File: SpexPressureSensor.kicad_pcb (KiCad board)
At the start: 2 copper layers, 51 x 51 mm, 62 parts, among them J1 3PinJumper, J2 edgeMountSMA, P1 CONN_6, P2 NICHROME, P3 TC2030-CTX, Q1 IRLL3303PbF, Q2 MOS_N_numbered, Q3 MOS_N_numbered, Q4 MMBT4403, Q5 MOS_N_numbered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

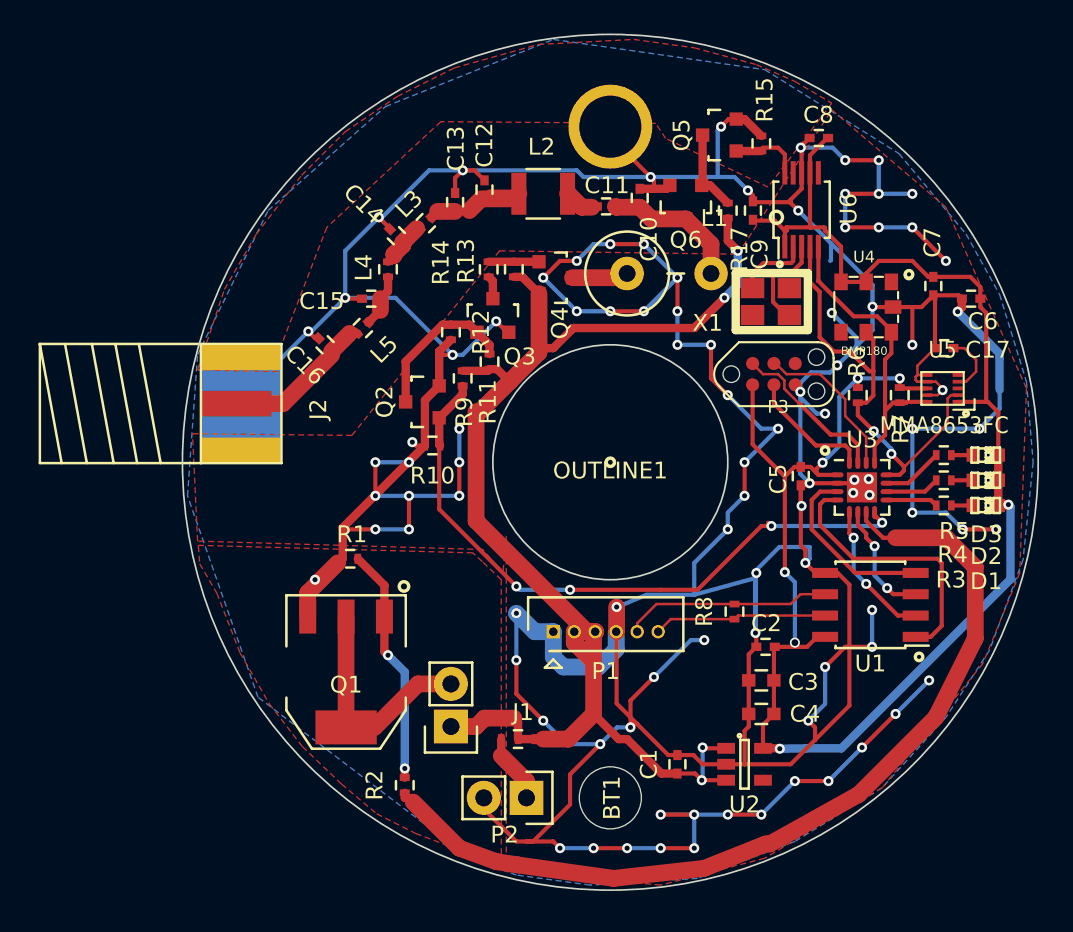
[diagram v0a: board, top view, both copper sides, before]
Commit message: Moved some traces around.
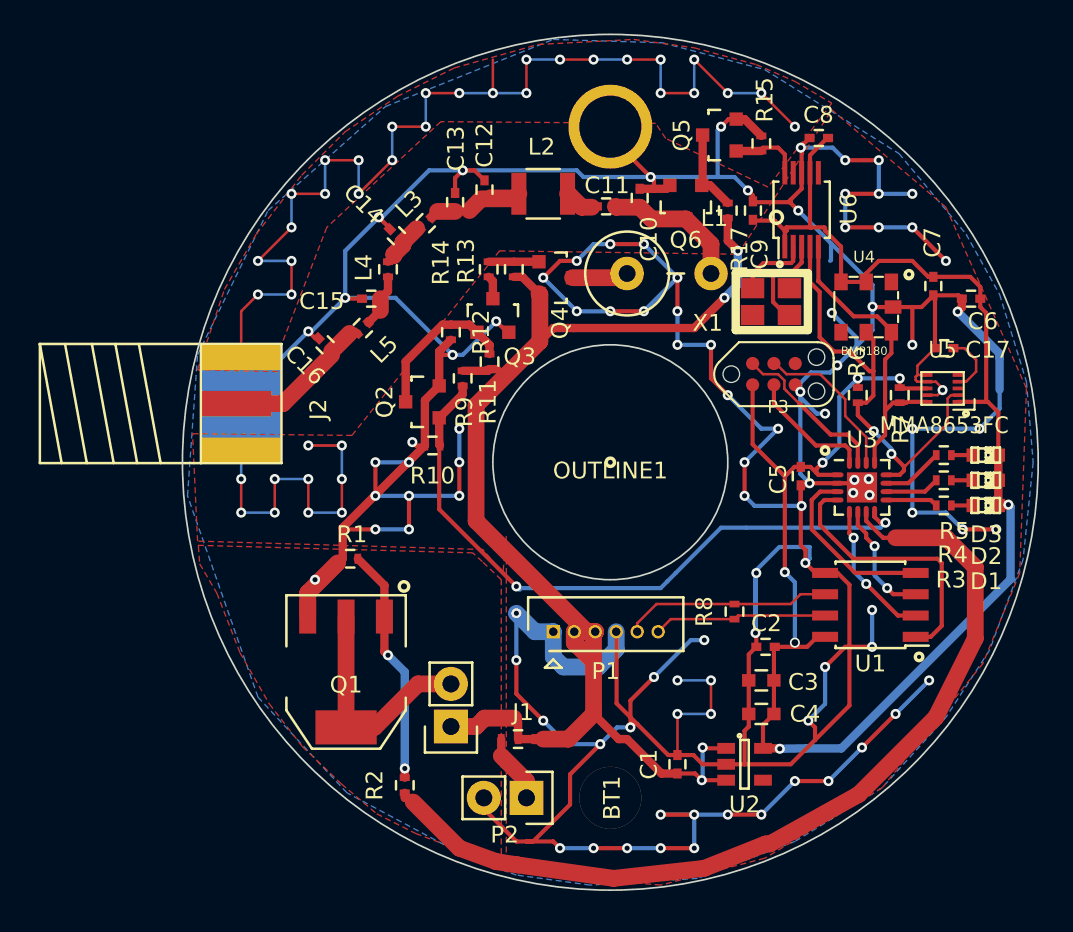
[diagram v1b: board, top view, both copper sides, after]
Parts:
- OUTLINE1: footprint PlugOutline:PLUG_OUTLINE -> PLUG_OUTLINE
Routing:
- net GND: track 414.7 -> 494.8 mm, vias 95 -> 135
- net /Beacon/12V: track 73.3 -> 71.9 mm
- net /Beacon/KEY: track 39.4 -> 40.0 mm, vias 4 -> 2

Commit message: Added a current monitor on the nichrome.
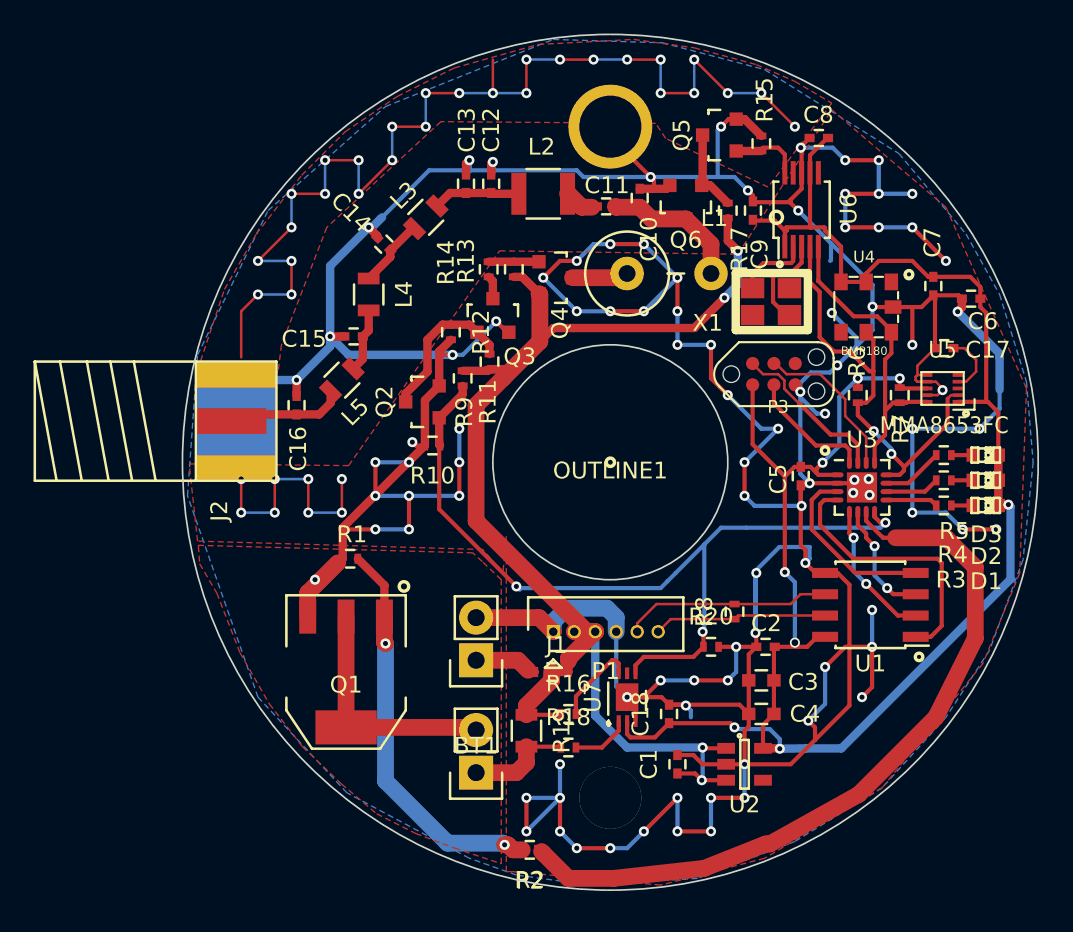
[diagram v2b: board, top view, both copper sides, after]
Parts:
- added C18: C, Capacitors_SMD:C_0402, F.Cu at (123.5, 80.0)
- added R16: R, Resistors_SMD:R_0402, F.Cu at (117.5, 80.0)
- added R18: R, Resistors_SMD:R_0402, F.Cu at (117.5, 82.0)
- added R19: R, Resistors_SMD:R_0805, F.Cu at (115.0, 81.0)
- added R20: R, Resistors_SMD:R_0402, F.Cu at (126.0, 76.0)
- added U7: LT6105, LT6105:LT6105, F.Cu at (121.0, 79.0)
- C17: value C -> 1uf
- L3, L4, L5: footprint Resistors_SMD:R_0402 -> Resistors_SMD:R_0805
- OUTLINE1: footprint PLUG_OUTLINE -> PlugOutline:PLUG_OUTLINE
- moved BT1 8.73 mm to (112.0, 76.8), turned to 180 degrees
- moved R2 8.39 mm to (115.2, 88.1), turned to 180 degrees
- moved J1 4.47 mm to (117.0, 77.5)
- moved C16 3.98 mm to (101.3, 61.6), turned to 90 degrees
- moved L5 3.34 mm to (104.0, 60.1)
- moved P2 3.13 mm to (112.0, 83.5)
- moved C15 2.48 mm to (104.7, 57.5)
- moved L4 1.89 mm to (105.6, 55.0)
- moved C13 1.28 mm to (111.4, 48.4)
- moved J2 1.09 mm to (93.7, 59.8)
- moved C14 0.90 mm to (106.5, 52.0)
- moved C12 0.53 mm to (112.9, 48.4)
- moved L3 0.35 mm to (109.0, 50.4)
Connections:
- P2 pad 1: Net-(J1-Pad2) -> Net-(P2-Pad1)
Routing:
- net GND: track 494.8 -> 403.1 mm, vias 135 -> 102
- net (no net): track 0.00 -> 63.5 mm, vias 0 -> 28
- net +3.3V: track 109.1 -> 120.4 mm, vias 7 -> 8
- net /Beacon/KEY: track 40.0 -> 51.1 mm, vias 2 -> 3
- net Net-(Q1-Pad1): track 14.5 -> 23.8 mm
- net Net-(R2-Pad1): track 54.1 -> 45.2 mm
- net Net-(P2-Pad1): track 0.00 -> 6.27 mm
- net Net-(R16-Pad2): track 0.00 -> 5.15 mm
- net Net-(R18-Pad2): track 0.00 -> 3.54 mm
- net Net-(C12-Pad1): track 8.00 -> 5.22 mm
- net Net-(J1-Pad2): track 5.31 -> 7.91 mm
- net Net-(P2-Pad2): track 13.9 -> 16.4 mm
- net /Beacon/12V: track 71.9 -> 74.2 mm
- net Net-(C16-Pad1): track 9.10 -> 7.08 mm
- net Net-(BT1-Pad1): track 5.12 -> 3.79 mm
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
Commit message: Realized the board was tooooo big.
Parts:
- removed BT1: BATTERY, Pin_Headers:Pin_Header_Straight_1x02
- removed C10: 47p, Capacitors_SMD:C_0402
- removed C11: 100p, Capacitors_SMD:C_0402
- removed C12: 56p, Capacitors_SMD:C_0402
- removed C13, C16: 150p, Capacitors_SMD:C_0402
- removed C14, C15: 220p, Capacitors_SMD:C_0402
- removed C17, C6, C8: 1uf, Capacitors_SMD:C_0402
- removed C9: .47uf, Capacitors_SMD:C_0402
- removed D2, D3: LED, LEDs:LED-0603
- removed G***: LOGO, spexLogo:logoBig
- removed J1: 3PinJumper, solderJmp:3solderJmp
- removed J2: edgeMountSMA, edgeSMA:EdgeSMA
- removed L1: INDUCTOR_SMALL, Resistors_ThroughHole:Resistor_Vertical_RM5mm
- removed L2: 4uh, Resistors_SMD:R_1210
- removed L3, L5: 390n, Resistors_SMD:R_0805
- removed L4: 470n, Resistors_SMD:R_0805
- removed Q2, Q3, Q5, Q6: MOS_N_numbered, Housings_SOT-23_SOT-143_TSOT-6:SOT-23
- removed Q4: MMBT4403, Housings_SOT-23_SOT-143_TSOT-6:SOT-23
- removed R10: DNP, Resistors_SMD:R_0402
- removed R11: 2K, Resistors_SMD:R_0402
- removed R12, R9: 10K, Resistors_SMD:R_0402
- removed R13, R14: 1K, Resistors_SMD:R_0402
- removed R15: 2000, Resistors_SMD:R_0402
- removed R17: R, Resistors_SMD:R_0402
- removed R4, R5: 100, Resistors_SMD:R_0402
- removed U5: MMA8653FC, MMA8653FC:MMA8653FCR1
- removed U6: SI5351A, Housings_SSOP:MSOP-10_3x3mm_Pitch0.5mm
- removed X1: NX3225GA, NX3225GA:NX3225GA
- C18, P3, U2, U3: moved to B.Cu
- U1: footprint Housings_SOIC:SOIC-8_3.9x4.9mm_Pitch1.27mm -> Housings_DFN_QFN:DFN-8-1EP_3x3mm_Pitch0.5mm
- moved R2 30.6 mm to (113.3, 57.5)
- moved C7 23.7 mm to (116.2, 60.2)
- moved U2 16.7 mm to (130.6, 66.5)
- moved Q1 15.5 mm to (111.2, 63.6)
- moved R1 14.6 mm to (111.0, 57.6)
- moved D1 11.9 mm to (131.1, 63.8)
- moved P2 11.3 mm to (112.5, 72.2), turned to 225 degrees
- moved U1 11.2 mm to (126.3, 67.0), turned to 315 degrees
- moved R19 11.2 mm to (116.2, 69.8), turned to 180 degrees
- moved R3 10.9 mm to (130.4, 62.2)
- moved C18 10.3 mm to (115.4, 73.7), turned to 0 degrees
- moved U3 10.2 mm to (125.8, 62.2), turned to 180 degrees
- moved R18 9.97 mm to (115.7, 72.2), turned to 270 degrees
- moved U4 9.60 mm to (125.7, 56.0)
- moved R7 8.79 mm to (128.9, 58.1), turned to 90 degrees
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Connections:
- net /Beacon/KEY renamed /NichromeI
- net /Beacon/SCL renamed Net-(R6-Pad2)
- net /Beacon/SDA renamed Net-(R7-Pad2)
- C1 pad 1: /Beacon/12V -> /VInput
- P1 pad 2: /Beacon/12V -> /VInput
- P1 pad 3: /Beacon/12V -> /VInput
- R16 pad 1: Net-(J1-Pad2) -> /VInput
- R19 pad 1: Net-(J1-Pad2) -> /VInput
- U2 pad 1: /Beacon/12V -> /VInput
- U2 pad 3: /Beacon/12V -> /VInput
- U3 pad 10: Net-(R4-Pad2) -> (no net)
- U3 pad 11: Net-(R5-Pad2) -> (no net)
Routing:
- net GND: track 403.1 -> 0.00 mm, vias 102 -> 0
- net +3.3V: track 120.4 -> 0.00 mm, vias 8 -> 0
- net /Beacon/12V: track 74.2 -> 0.00 mm, vias 4 -> 0
- net (no net): track 63.5 -> 0.00 mm, vias 28 -> 0
- net /NichromeI: track 51.1 -> 0.00 mm, vias 3 -> 0
- net Net-(R2-Pad1): track 45.2 -> 0.00 mm
- net Net-(R6-Pad2): track 27.0 -> 0.00 mm, vias 2 -> 0
- net Net-(Q1-Pad1): track 23.8 -> 0.00 mm, vias 2 -> 0
- net Net-(R7-Pad2): track 18.7 -> 0.00 mm
- net Net-(P2-Pad2): track 16.4 -> 0.00 mm
- net Net-(U1-Pad1): track 16.1 -> 0.00 mm
- net Net-(P1-Pad5): track 12.4 -> 0.00 mm
- net Net-(U1-Pad4): track 10.8 -> 0.00 mm
- net Net-(P1-Pad6): track 10.4 -> 0.00 mm
- net /SWDIO: track 9.65 -> 0.00 mm
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- removed copper zone on B.Cu, net GND
- removed copper zone on F.Cu, net GND
- removed copper zone on F.Cu, net Net-(P2-Pad2)
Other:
- board outline removed

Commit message: Finished board. Ready to go. Should add gerbers.
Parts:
- C1, C3, C4, R6, R7, R8: moved to B.Cu
- C18, P3: moved to F.Cu
- moved C4 16.2 mm to (130.9, 63.9)
- moved C3 15.9 mm to (130.9, 62.2)
- moved R6 15.9 mm to (113.9, 55.9)
- moved C1 15.4 mm to (129.9, 68.8), turned to 0 degrees
- moved R7 13.8 mm to (115.4, 55.9), turned to 270 degrees
- moved P3 11.2 mm to (123.2, 53.5), turned to 315 degrees
- moved U4 11.1 mm to (114.5, 56.0)
- moved C7 6.28 mm to (111.8, 55.8)
- moved R2 3.77 mm to (116.0, 60.1)
- moved R8 3.61 mm to (130.1, 71.5), turned to 225 degrees
- moved C18 2.94 mm to (113.2, 75.7), turned to 270 degrees
- moved U3 2.47 mm to (126.0, 59.8)
- moved R3 2.02 mm to (128.9, 63.6)
- moved R1 1.46 mm to (109.5, 58.0)
- moved D1 1.05 mm to (132.0, 63.4)
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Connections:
- R2 pad 1: Net-(R2-Pad1) -> /cut
- U1 pad 9: (no net) -> GND
- U3 pad 11: (no net) -> /cut
- U3 pad 7: Net-(R2-Pad1) -> (no net)
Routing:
- net GND: track 0.00 -> 204.3 mm, vias 0 -> 54
- net +3.3V: track 0.00 -> 74.8 mm, vias 0 -> 6
- net /VInput: track 0.00 -> 23.9 mm
- net /NichromeI: track 0.00 -> 19.8 mm, vias 0 -> 1
- net Net-(R6-Pad2): track 0.00 -> 14.4 mm, vias 0 -> 1
- net Net-(R7-Pad2): track 0.00 -> 14.3 mm, vias 0 -> 1
- net Net-(U1-Pad4): track 0.00 -> 13.8 mm, vias 0 -> 1
- net Net-(P2-Pad2): track 0.00 -> 10.4 mm
- net /cut: track 0.00 -> 8.99 mm, vias 0 -> 1
- net /SWDIO: track 0.00 -> 8.70 mm, vias 0 -> 1
- net Net-(R3-Pad2): track 0.00 -> 7.52 mm, vias 0 -> 1
- net Net-(U1-Pad1): track 0.00 -> 7.29 mm, vias 0 -> 1
- net Net-(Q1-Pad1): track 0.00 -> 6.89 mm
- net /RESET: track 0.00 -> 6.62 mm, vias 0 -> 1
- net /SWCLK: track 0.00 -> 6.56 mm, vias 0 -> 1
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- added copper zone on B.Cu, net GND
- added copper zone on F.Cu, net GND
- added copper zone on F.Cu, net Net-(P2-Pad2)
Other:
- board outline added: 28 x 28 mm
- board text added: "Tigris ad Astra AB1TJ Nov 2016 Spex Pressure Sensor"
- board text removed: "Tigris ad Astra AB1TJ Nov 2015 Spex Pressure Sensor"
